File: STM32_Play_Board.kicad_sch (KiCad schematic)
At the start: 1 part, among them U1 STM32C031C6T6

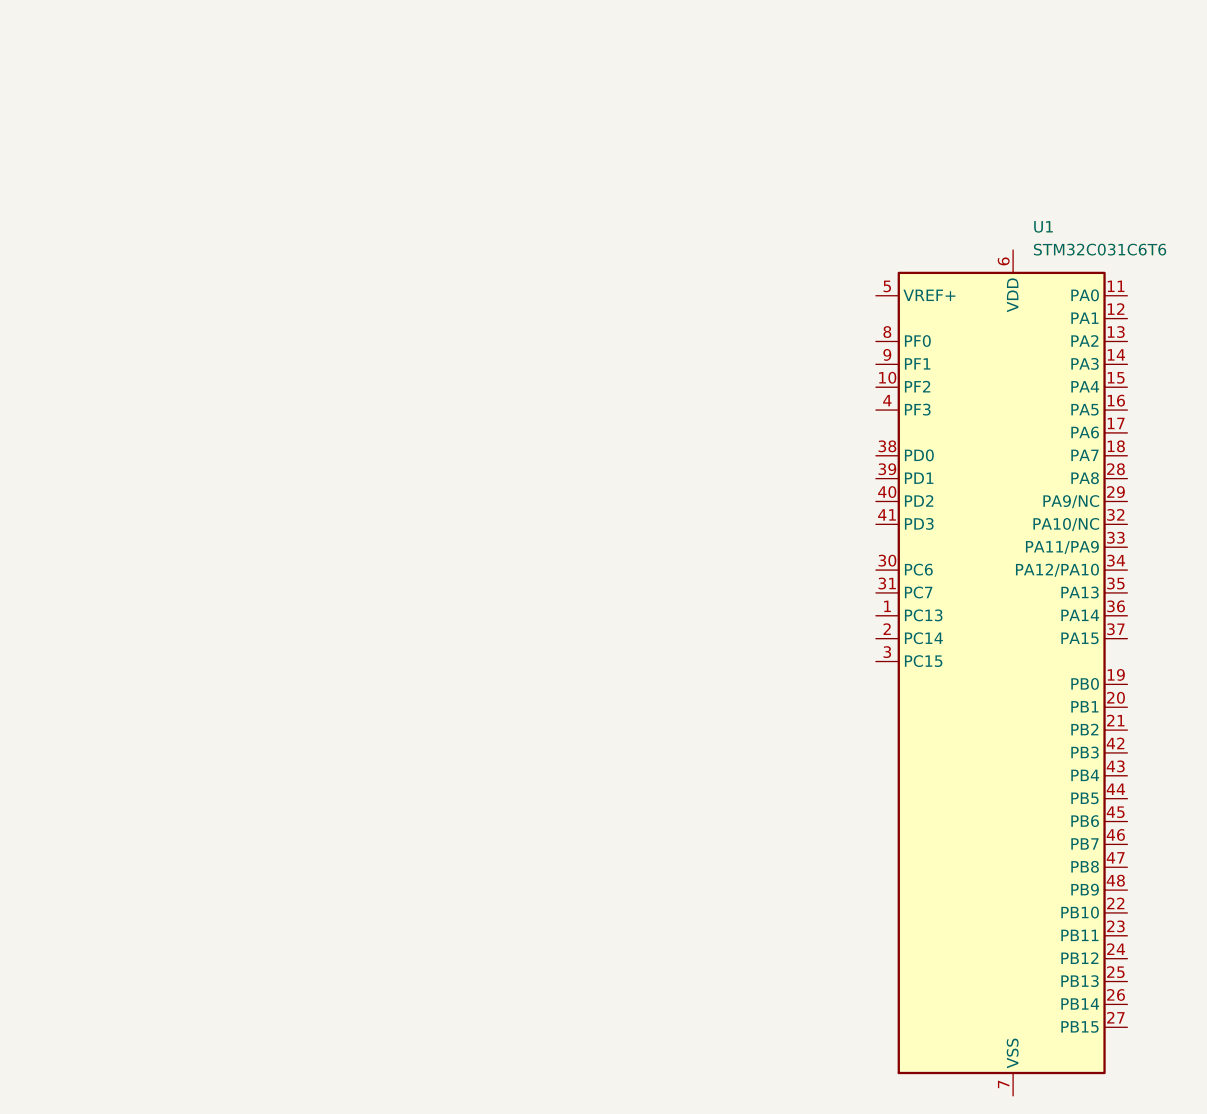
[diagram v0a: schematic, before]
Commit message: added components and schematics
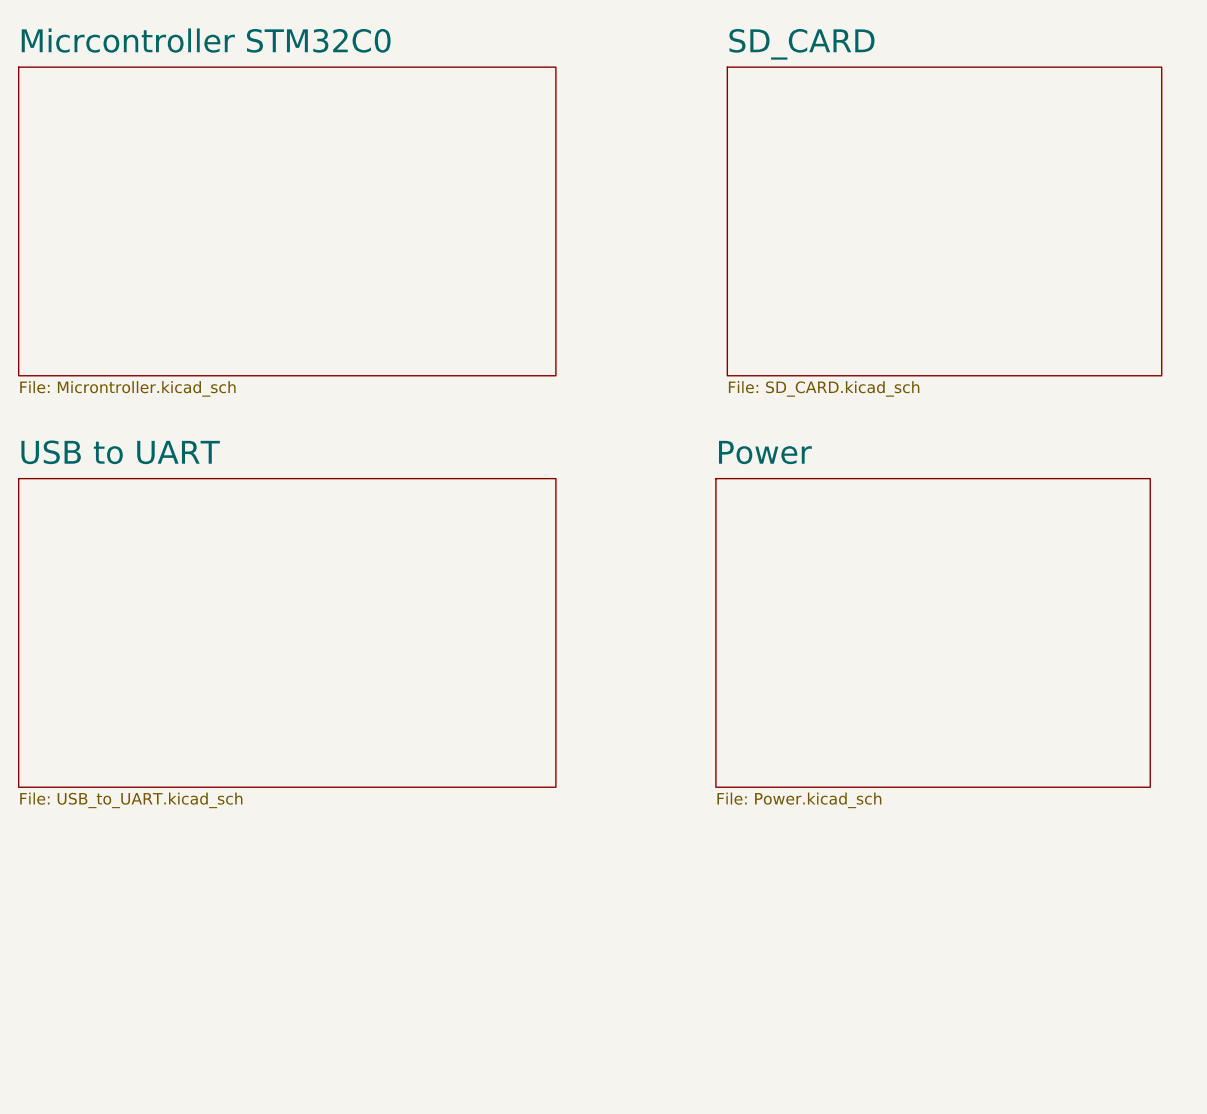
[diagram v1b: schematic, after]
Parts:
- removed U1: STM32C031C6T6, Package_QFP:LQFP-48_7x7mm_P0.5mm, symbol MCU_ST_STM32C0:STM32C031C6Tx
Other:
- added sheet Micrcontroller STM32C0 (Microntroller.kicad_sch)
- added sheet Power (Power.kicad_sch)
- added sheet SD_CARD (SD_CARD.kicad_sch)
- added sheet USB to UART (USB_to_UART.kicad_sch)
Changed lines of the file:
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@@
 		(company "Ground Loops")
 	)
-	(symbol
-		(lib_id "MCU_ST_STM32C0:STM32C031C6Tx")
-		(at 140.97 96.52 0)
-		(unit 1)
-		(exclude_from_sim no)
-		(in_bom yes)
-		(on_board yes)
-		(dnp no)
+	(sheet
+		(at 111.76 27.94)
+		(size 48.26 34.29)
 		(fields_autoplaced yes)
-		(property "Reference" "U1"
-			(at 145.7041 45.72 0)
+		(stroke
+			(width 0.1524)
+			(type solid)
+		)
+		(fill
+			(color 26 42 255 1.0000)
+		)
+		(property "Sheetname" "SD_CARD"
+			(at 111.76 26.5934 0)
+			(effects
+				(font
+					(size 2.54 2.54)
+				)
+				(justify left bottom)
+			)
+		)
+		(property "Sheetfile" "SD_CARD.kicad_sch"
+			(at 111.76 62.8146 0)
 			(effects
 				(font
 					(size 1.27 1.27)
 				)
-				(justify left)
+				(justify left top)
 			)
 		)
-		(property "Value" "STM32C031C6T6"
-			(at 145.7041 48.26 0)
+		(instances
+			(project "STM32_Play_Board"
+				(path "/9848a691-cd53-4e57-940a-e5db2e63f9a1"
+					(page "4")
+				)
+			)
+		)
+	)
+	(sheet
+		(at 33.02 73.66)
+		(size 59.69 34.29)
+		(fields_autoplaced yes)
+		(stroke
+			(width 0.1524)
+			(type solid)
+		)
+		(fill
+			(color 26 42 255 1.0000)
+		)
+		(property "Sheetname" "USB to UART"
+			(at 33.02 72.3134 0)
+			(effects
+				(font
+					(size 2.54 2.54)
+				)
+				(justify left bottom)
+			)
+		)
+		(property "Sheetfile" "USB_to_UART.kicad_sch"
+			(at 33.02 108.5346 0)
 			(effects
 				(font
 					(size 1.27 1.27)
 				)
-				(justify left)
+				(justify left top)
 			)
 		)
-		(property "Footprint" "Package_QFP:LQFP-48_7x7mm_P0.5mm"
-			(at 130.81 139.7 0)
+		(instances
+			(project "STM32_Play_Board"
+				(path "/9848a691-cd53-4e57-940a-e5db2e63f9a1"
+					(page "3")
+				)
+			)
+		)
+	)
+	(sheet
+		(at 33.02 27.94)
+		(size 59.69 34.29)
+		(fields_autoplaced yes)
+		(stroke
+			(width 0.1524)
+			(type solid)
+		)
+		(fill
+			(color 196 26 255 1.0000)
+		)
+		(property "Sheetname" "Micrcontroller STM32C0"
+			(at 33.02 26.5934 0)
+			(effects
+				(font
+					(size 2.54 2.54)
+				)
+				(justify left bottom)
+			)
+		)
+		(property "Sheetfile" "Microntroller.kicad_sch"
+			(at 33.02 62.8146 0)
 			(effects
 				(font
 					(size 1.27 1.27)
 				)
-				(justify right)
-				(hide yes)
+				(justify left top)
 			)
 		)
-		(property "Datasheet" "https://www.st.com/resource/en/datasheet/stm32c031c6.pdf"
-			(at 140.97 96.52 0)
+		(instances
+			(project "STM32_Play_Board"
+				(path "/9848a691-cd53-4e57-940a-e5db2e63f9a1"
+					(page "2")
+				)
+			)
+		)
+	)
+	(sheet
+		(at 110.49 73.66)
+		(size 48.26 34.29)
+		(fields_autoplaced yes)
+		(stroke
+			(width 0.1524)
+			(type solid)
+		)
+		(fill
+			(color 144 255 52 1.0000)
+		)
+		(property "Sheetname" "Power"
+			(at 110.49 72.3134 0)
+			(effects
+				(font
+					(size 2.54 2.54)
+				)
+				(justify left bottom)
+			)
+		)
+		(property "Sheetfile" "Power.kicad_sch"
+			(at 110.49 108.5346 0)
 			(effects
 				(font
 					(size 1.27 1.27)
 				)
-				(hide yes)
+				(justify left top)
 			)
-		)
-		(property "Description" "STMicroelectronics Arm Cortex-M0+ MCU, 32KB flash, 12KB RAM, 48 MHz, 2.0-3.6V, 45 GPIO, LQFP48"
-			(at 140.97 96.52 0)
-			(effects
-				(font
-					(size 1.27 1.27)
-				)
-				(hide yes)
-			)
-		)
-		(pin "10"
-		)
-		(pin "12"
-		)
-		(pin "19"
-		)
-		(pin "22"
-		)
-		(pin "23"
-		)
-		(pin "26"
-		)
-		(pin "3"
-		)
-		(pin "15"
-		)
-		(pin "16"
-		)
-		(pin "31"
-		)
-		(pin "21"
-		)
-		(pin "20"
-		)
-		(pin "33"
-		)
-		(pin "34"
-		)
-		(pin "14"
-		)
-		(pin "1"
-		)
-		(pin "17"
-		)
-		(pin "24"
-		)
-		(pin "30"
-		)
-		(pin "35"
-		)
-		(pin "5"
-		)
-		(pin "28"
-		)
-		(pin "18"
-		)
-		(pin "25"
-		)
-		(pin "32"
-		)
-		(pin "36"
-		)
-		(pin "11"
-		)
-		(pin "13"
-		)
-		(pin "29"
-		)
-		(pin "2"
-		)
-		(pin "37"
-		)
-		(pin "27"
-		)
-		(pin "47"
-		)
-		(pin "43"
-		)
-		(pin "42"
-		)
-		(pin "8"
-		)
-		(pin "4"
-		)
-		(pin "48"
-		)
-		(pin "41"
-		)
-		(pin "45"
-		)
-		(pin "6"
-		)
-		(pin "39"
-		)
-		(pin "38"
-		)
-		(pin "40"
-		)
-		(pin "46"
-		)
-		(pin "7"
-		)
-		(pin "9"
-		)
-		(pin "44"
 		)
 		(instances
 			(project "STM32_Play_Board"
 				(path "/9848a691-cd53-4e57-940a-e5db2e63f9a1"
-					(reference "U1")
-					(unit 1)
+					(page "5")
 				)
 			)

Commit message: dfvdfv
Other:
- added sheet Voltage and Current Measurement (Voltage_and_Current_Measurement.kicad_sch)
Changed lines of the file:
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@@
+	)
+	(sheet
+		(at 175.26 27.94)
+		(size 48.26 33.02)
+		(fields_autoplaced yes)
+		(stroke
+			(width 0.1524)
+			(type solid)
+		)
+		(fill
+			(color 22 180 177 1.0000)
+		)
+		(property "Sheetname" "Voltage and Current Measurement"
+			(at 175.26 26.5934 0)
+			(effects
+				(font
+					(size 2.54 2.54)
+				)
+				(justify left bottom)
+			)
+		)
+		(property "Sheetfile" "Voltage_and_Current_Measurement.kicad_sch"
+			(at 175.26 61.5446 0)
+			(effects
+				(font
+					(size 1.27 1.27)
+				)
+				(justify left top)
+			)
+		)
+		(instances
+			(project "STM32_Play_Board"
+				(path "/9848a691-cd53-4e57-940a-e5db2e63f9a1"
+					(page "6")
+				)
+			)
+		)
 	)
 	(sheet

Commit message: changes to schematic and PCB
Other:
- added sheet Connectors (Connectors.kicad_sch)
- sheet Micrcontroller STM32C0 ports: added +3V3_Meas, -3V3_Supply, Curr_meas, PA11/PA9, PA12/PA10, PA13, PA14, PA7, PB1, PB10, PB11, PB12, PB13, PB14, PB15, PB2, PB6, PB7, PB8, PB9, PC13, PC14, PC15, PC6, PC7, PD0, PD1, PD2, PD3, PF3, SPI_Clk, SPI_Cs, SPI_Miso, SPI_Mosi, UART1_Rx, UART1_Tx, UART2_Rx, UART2_Tx, Volt_meas, i_Supply; removed none
- sheet Power ports: added +3V3_Meas, -3V3_Supply, i_Supply; removed none
- sheet SD_CARD ports: added SPI_Clk, SPI_Cs, SPI_Miso, SPI_Mosi; removed none
- sheet USB to UART ports: added UART1_Rx, UART1_Tx; removed none
- sheet Voltage and Current Measurement ports: added Curr_meas, Volt_meas; removed none

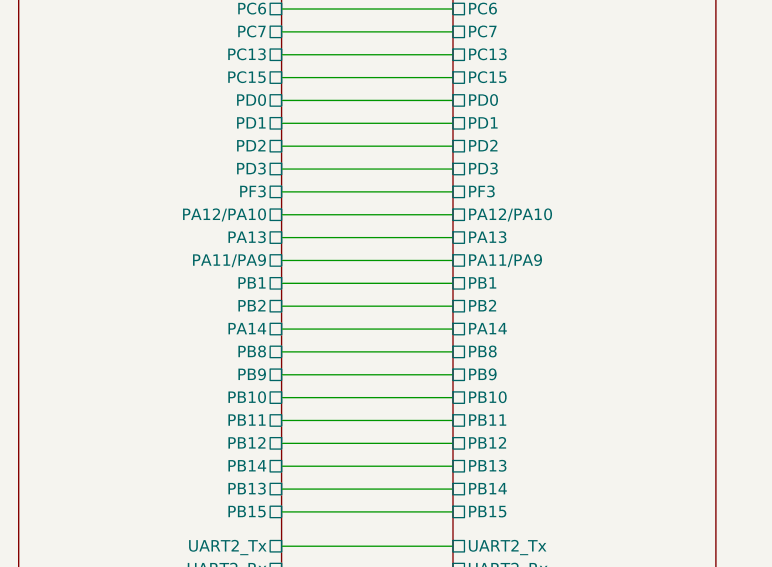
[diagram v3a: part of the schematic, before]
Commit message: changed schematics
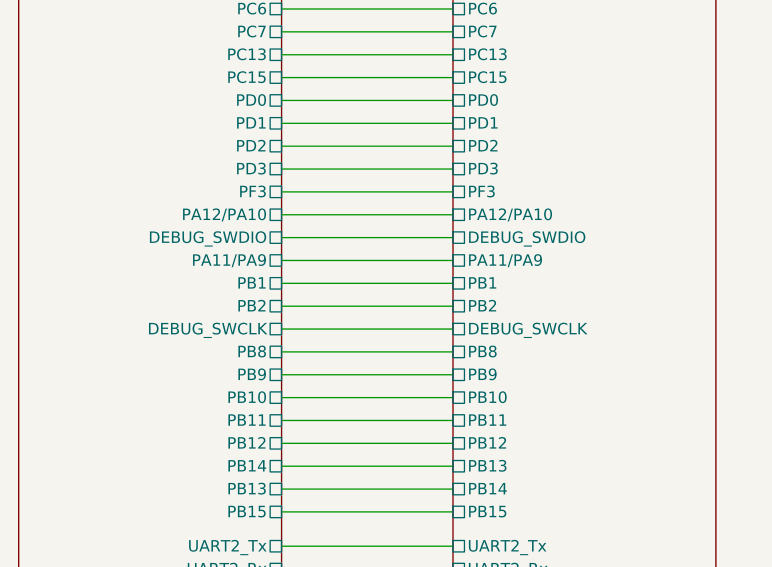
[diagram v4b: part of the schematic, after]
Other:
- sheet Connectors ports: added DEBUG_SWCLK, DEBUG_SWDIO; removed PA13, PA14
- sheet Micrcontroller STM32C0 ports: added DEBUG_SWCLK, DEBUG_SWDIO; removed PA13, PA14
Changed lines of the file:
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@@
-			)
-		)
-		(pin "PA13" passive
-			(at 80.01 59.69 180)
-			(effects
-				(font
-					(size 1.27 1.27)
-				)
-				(justify left)
 			)
 		)
@@
 			)
 		)
-		(pin "PA14" passive
-			(at 80.01 69.85 180)
-			(effects
-				(font
-					(size 1.27 1.27)
-				)
-				(justify left)
-			)
-		)
 		(pin "PA12{slash}PA10" passive
 			(at 80.01 57.15 180)
@@
 		(pin "UART2_Rx" passive
 			(at 80.01 96.52 180)
+			(effects
+				(font
+					(size 1.27 1.27)
+				)
+				(justify left)
+			)
+		)
+		(pin "DEBUG_SWDIO" passive
+			(at 80.01 59.69 180)
+			(effects
+				(font
+					(size 1.27 1.27)
+				)
+				(justify left)
+			)
+		)
+		(pin "DEBUG_SWCLK" passive
+			(at 80.01 69.85 180)
 			(effects
 				(font
@@
 			)
 		)
-		(pin "PA13" passive
-			(at 60.96 59.69 0)
-			(effects
-				(font
-					(size 1.27 1.27)
-				)
-				(justify right)
-			)
-		)
 		(pin "PA11{slash}PA9" passive
 			(at 60.96 62.23 0)
@@
 			)
 		)
-		(pin "PA14" passive
-			(at 60.96 69.85 0)
-			(effects
-				(font
-					(size 1.27 1.27)
-				)
-				(justify right)
-			)
-		)
 		(pin "PB8" passive
 			(at 60.96 72.39 0)
@@
 			(effects
 				(font
+					(size 1.27 1.27)
+				)
+				(justify right)
+			)
+		)
+		(pin "DEBUG_SWDIO" passive
+			(at 60.96 59.69 0)
+			(effects
+				(font
+					(size 1.27 1.27)
+				)
+				(justify right)
+			)
+		)
+		(pin "DEBUG_SWCLK" passive
+			(at 60.96 69.85 0)
+			(effects
+				(font
